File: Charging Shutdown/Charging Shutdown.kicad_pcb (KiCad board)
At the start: 2 copper layers, 47.4 x 52.9 mm, 13 parts, among them J2 776280-1, K1 PR2212V4001A, K3 PR2212V4001A, Q1 2N2222, Q3 2N2222

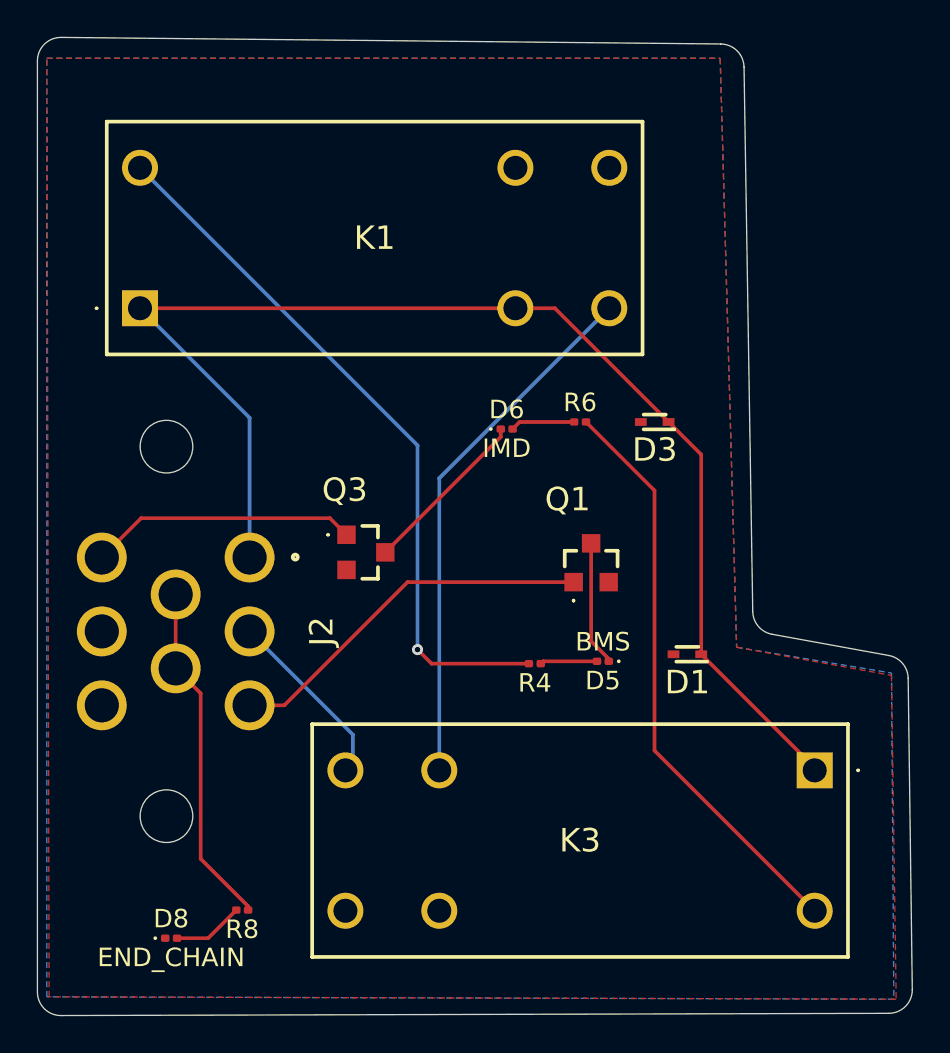
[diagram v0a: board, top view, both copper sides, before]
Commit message: Moved relay position
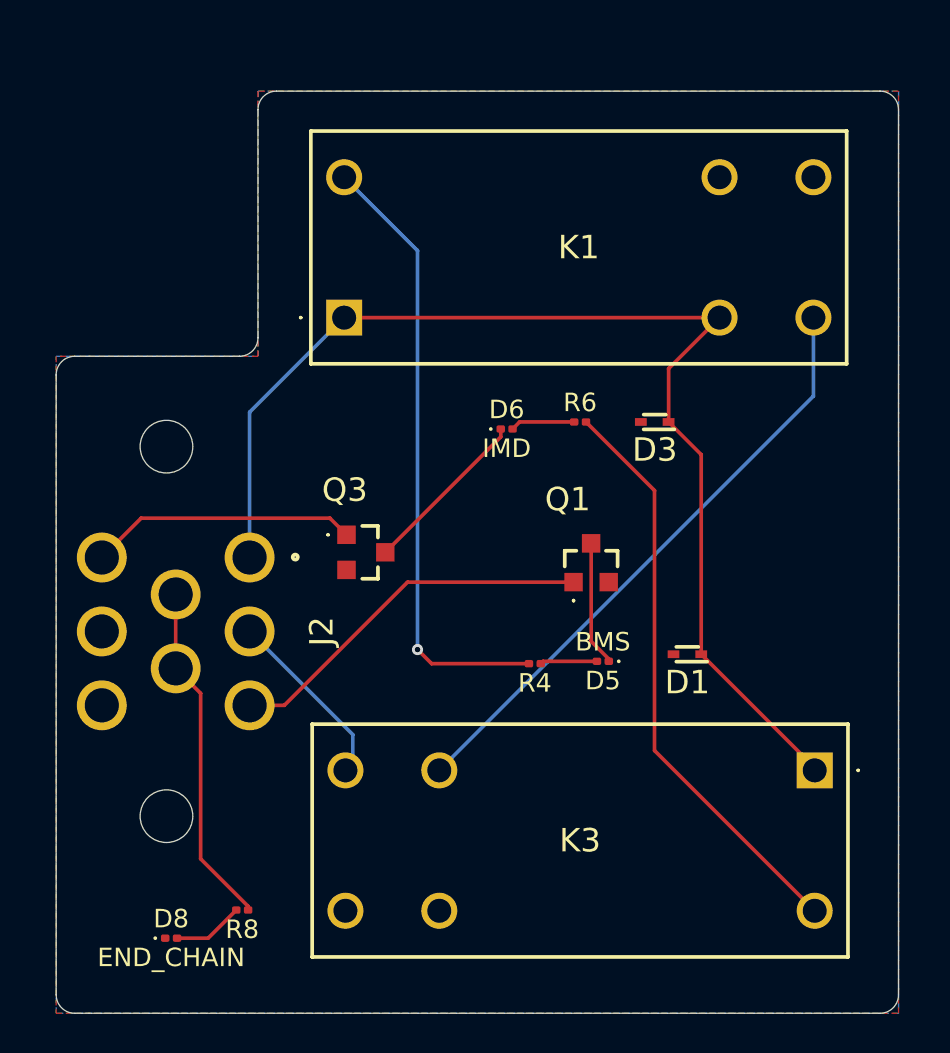
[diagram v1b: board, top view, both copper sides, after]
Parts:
- moved K1 11.1 mm to (98.1, 80.1)
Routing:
- net Net-(K1-COIL_2): track 38.6 -> 33.6 mm
- net +12V: track 68.9 -> 64.3 mm
- net Net-(K1-NO_1): track 28.8 -> 32.9 mm
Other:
- board size 47.4 x 52.9 mm -> 45.6 x 49.9 mm
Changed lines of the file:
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@@
-			)
-		)
-		(model "C:/Users/Schet/Downloads/New folder (2)/1_776280_1/KiCADv6/c-776280-1-h-3d.stp"
-			(offset
-				(xyz 0 -20 11.5)
-			)
-			(scale
-				(xyz 1 1 1)
-			)
-			(rotate
-				(xyz -90 -0 -0)
 			)
 		)
@@
 	(footprint "Shutdown_Footprint:PR2212V4001A"
 		(layer "F.Cu")
-		(at 87.087 79.569)
+		(at 98.136 80.077)
 		(descr "PR22-12V-400-1A-2")
 		(tags "Relay or Contactor")
@@
 			)
 		)
-		(model "C:/Users/Schet/Downloads/PR22_12V_400_1A/PR22-12V-400-1A.step"
-			(offset
-				(xyz 12 4 0)
-			)
-			(scale
-				(xyz 1 1 1)
-			)
-			(rotate
-				(xyz -90 -0 -0)
-			)
-		)
 	)
 	(footprint "Shutdown_Footprint:PR2212V4001A"
@@
 			)
 		)
-		(model "C:/Users/Schet/Downloads/PR22_12V_400_1A/PR22-12V-400-1A.step"
-			(offset
-				(xyz 12 4 0)
-			)
-			(scale
-				(xyz 1 1 1)
-			)
-			(rotate
-				(xyz -90 -0 -0)
-			)
-		)
 	)
 	(footprint "Diode_SMD:SODFL1608X70N"
@@
 		)
 	)
-	(gr_arc
-		(start 118.523616 65.265667)
-		(mid 119.406272 65.634874)
-		(end 119.780797 66.515287)
+	(gr_line
+		(start 82.55 83.169)
+		(end 82.55 116.729)
 		(stroke
 			(width 0.05)
@@
 		(layer "Edge.Cuts")
 	)
-	(gr_line
-		(start 82.807405 117.852586)
-		(end 127.621518 117.732441)
+	(gr_arc
+		(start 82.55 83.169)
+		(mid 82.842893 82.461893)
+		(end 83.55 82.169)
 		(stroke
 			(width 0.05)
@@
 		(layer "Edge.Cuts")
 	)
-	(gr_arc
-		(start 128.888002 116.445626)
-		(mid 128.523245 117.353267)
-		(end 127.621518 117.732441)
+	(gr_line
+		(start 83.55 82.169)
+		(end 84.328 82.169)
 		(stroke
 			(width 0.05)
@@
 		(layer "Edge.Cuts")
 	)
-	(gr_line
-		(start 120.252317 95.985342)
-		(end 119.780797 66.515287)
+	(gr_arc
+		(start 83.55 117.729)
+		(mid 82.842893 117.436107)
+		(end 82.55 116.729)
 		(stroke
 			(width 0.05)
@@
 	)
 	(gr_line
-		(start 118.523616 65.265667)
-		(end 82.816657 64.909784)
+		(start 83.55 117.729)
+		(end 84.328 117.729)
 		(stroke
 			(width 0.05)
@@
 	)
 	(gr_line
-		(start 127.622145 98.364936)
-		(end 121.29497 97.21454)
+		(start 84.328 117.729)
+		(end 127.143 117.729)
 		(stroke
 			(width 0.05)
@@
 		(layer "Edge.Cuts")
 	)
-	(gr_arc
-		(start 81.534 66.179721)
-		(mid 81.910461 65.277232)
-		(end 82.816657 64.909784)
+	(gr_line
+		(start 92.472 82.169)
+		(end 84.328 82.169)
 		(stroke
 			(width 0.05)
@@
 	)
 	(gr_line
-		(start 81.534 66.179721)
-		(end 81.534 116.582591)
+		(start 93.472 68.818)
+		(end 93.472 81.169)
 		(stroke
 			(width 0.05)
@@
 	)
 	(gr_arc
-		(start 121.29497 97.21454)
-		(mid 120.55365 96.786548)
-		(end 120.252317 95.985342)
+		(start 93.472 68.818)
+		(mid 93.764893 68.110893)
+		(end 94.472 67.818)
 		(stroke
 			(width 0.05)
@@
 		(layer "Edge.Cuts")
 	)
-	(gr_line
-		(start 128.888002 116.445626)
-		(end 128.664849 99.59763)
+	(gr_arc
+		(start 93.472 81.169)
+		(mid 93.179107 81.876107)
+		(end 92.472 82.169)
 		(stroke
 			(width 0.05)
@@
 		(layer "Edge.Cuts")
 	)
-	(gr_arc
-		(start 127.622145 98.364936)
-		(mid 128.364595 98.794262)
-		(end 128.664849 99.59763)
+	(gr_line
+		(start 127.143 67.818)
+		(end 94.472 67.818)
 		(stroke
 			(width 0.05)
@@
 	)
 	(gr_arc
-		(start 82.807405 117.852586)
-		(mid 81.907183 117.481819)
-		(end 81.534 116.582591)
+		(start 127.143 67.818)
+		(mid 127.850107 68.110893)
+		(end 128.143 68.818)
 		(stroke
 			(width 0.05)
@@
 		(layer "Edge.Cuts")
 	)
-	(segment
-		(start 109.541 79.569)
-		(end 107.407 79.569)
-		(width 0.2)
-		(layer "F.Cu")
-		(net 1)
+	(gr_arc
+		(start 128.143 116.729)
+		(mid 127.850107 117.436107)
+		(end 127.143 117.729)
+		(stroke
+			(width 0.05)
+			(type default)
+		)
+		(layer "Edge.Cuts")
+	)
+	(gr_line
+		(start 128.143 116.729)
+		(end 128.143 68.818)
+		(stroke
+			(width 0.05)
+			(type default)
+		)
+		(layer "Edge.Cuts")
 	)
 	(segment
@@
 	)
 	(segment
+		(start 118.456 80.077)
+		(end 115.697 82.836)
+		(width 0.2)
+		(layer "F.Cu")
+		(net 1)
+	)
+	(segment
+		(start 117.463 98.298)
+		(end 117.463 87.491)
+		(width 0.2)
+		(layer "F.Cu")
+		(net 1)
+	)
+	(segment
 		(start 117.463 87.491)
 		(end 115.697 85.725)
@@
 	)
 	(segment
-		(start 87.087 79.569)
-		(end 107.087 79.569)
+		(start 98.136 80.077)
+		(end 118.456 80.077)
 		(width 0.2)
 		(layer "F.Cu")
@@
 	)
 	(segment
-		(start 117.463 98.298)
-		(end 117.463 87.491)
+		(start 115.697 82.836)
+		(end 115.697 85.725)
 		(width 0.2)
 		(layer "F.Cu")
@@
 	)
 	(segment
-		(start 115.697 85.725)
-		(end 109.541 79.569)
-		(width 0.2)
-		(layer "F.Cu")
-		(net 1)
-	)
-	(segment
-		(start 87.087 79.569)
-		(end 93.019 85.501)
+		(start 93.019 85.194)
+		(end 98.136 80.077)
 		(width 0.2)
 		(layer "B.Cu")
@@
 	)
 	(segment
-		(start 93.019 85.501)
-		(end 93.019 93.061)
+		(start 93.019 93.061)
+		(end 93.019 85.194)
 		(width 0.2)
 		(layer "B.Cu")
@@
 	)
 	(segment
-		(start 103.286 104.581)
-		(end 103.286 88.77)
+		(start 123.536 84.331)
+		(end 103.286 104.581)
 		(width 0.2)
 		(layer "B.Cu")
@@
 	)
 	(segment
-		(start 103.286 88.77)
-		(end 112.487 79.569)
+		(start 123.536 80.077)
+		(end 123.536 84.331)
 		(width 0.2)
 		(layer "B.Cu")
@@
 	)
 	(segment
-		(start 102.108 98.044)
-		(end 102.108 86.99)
+		(start 102.108 76.449)
+		(end 102.108 98.044)
 		(width 0.2)
 		(layer "B.Cu")
@@
 	)
 	(segment
-		(start 102.108 86.99)
-		(end 87.087 71.969)
+		(start 98.136 72.477)
+		(end 102.108 76.449)
 		(width 0.2)
 		(layer "B.Cu")
@@
 		(polygon
 			(pts
-				(xy 82.042 66.04) (xy 118.491 66.04) (xy 119.38 97.917) (xy 127.762 99.441) (xy 128.016 116.967)
-				(xy 82.169 116.84)
+				(xy 82.55 82.169) (xy 82.55 117.729) (xy 128.143 117.729) (xy 128.143 67.818) (xy 93.472 67.818)
+				(xy 93.472 82.169)
 			)
 		)
@@
 		(polygon
 			(pts
-				(xy 82.042 66.04) (xy 118.491 66.04) (xy 119.38 97.917) (xy 127.762 99.314) (xy 127.889 116.967)
-				(xy 82.042 116.84)
-			)
-		)
+				(xy 82.55 82.169) (xy 93.472 82.169) (xy 93.472 67.818) (xy 128.143 67.818) (xy 128.143 117.729)
+				(xy 82.55 117.729)
+			)
+		)
